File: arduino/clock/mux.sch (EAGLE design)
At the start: 53 parts, among them U1 SN74HC595N, U2 SN74HC595N, U3 SN74HC595N

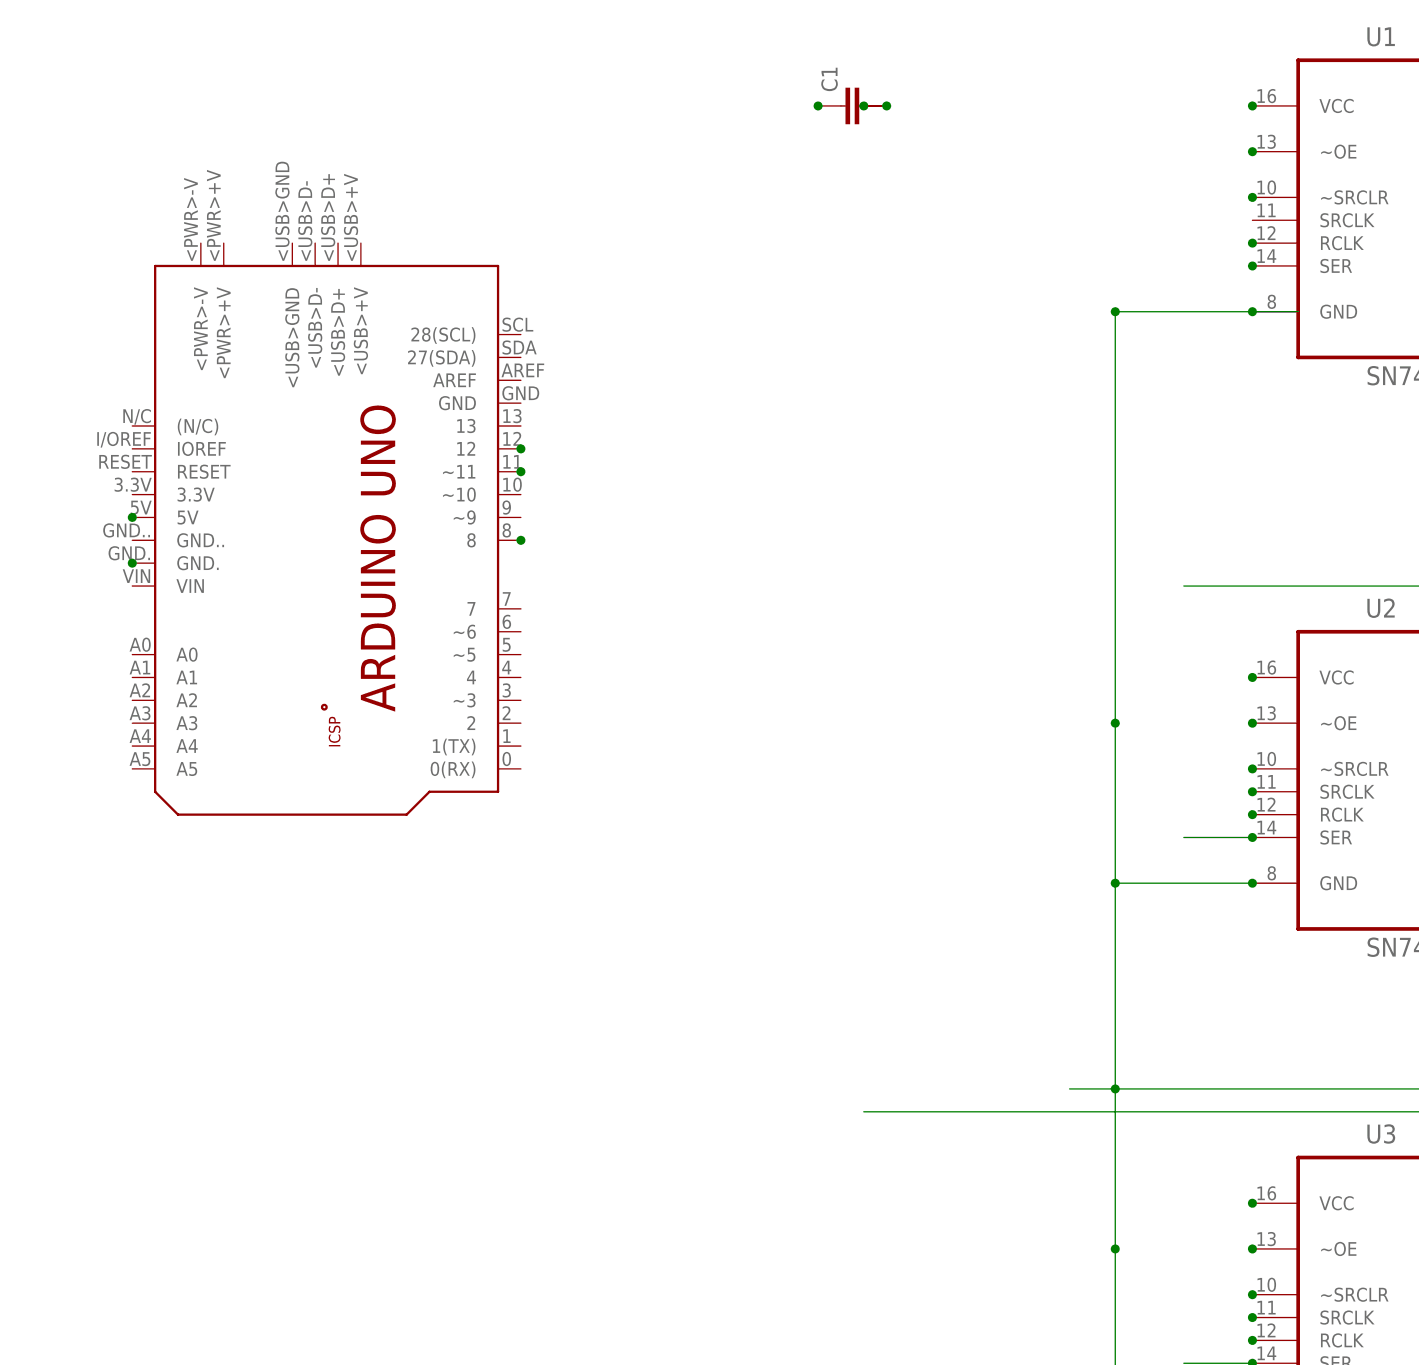
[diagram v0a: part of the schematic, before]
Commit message: Rewire +5V => VCC U{1,2,3}
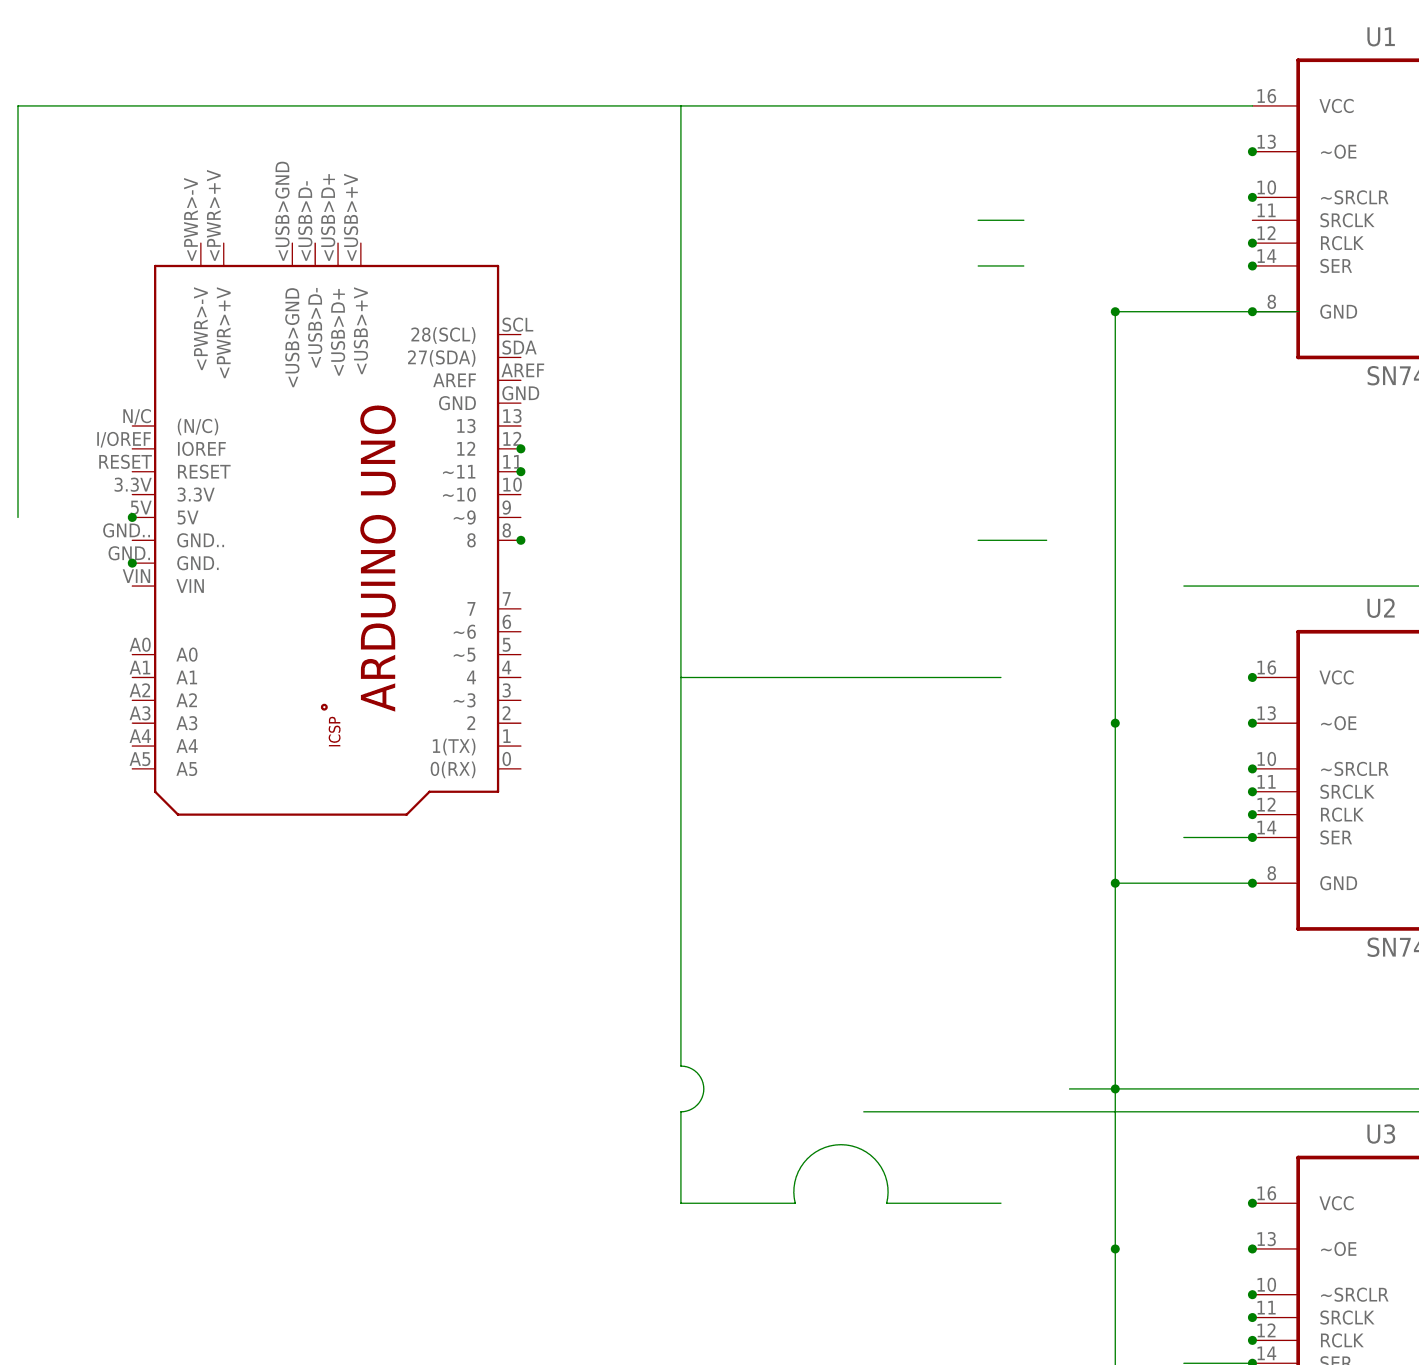
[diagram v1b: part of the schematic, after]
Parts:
- removed C1: (no value), capacitor-wima:C-10-15/6
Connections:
- removed net N$50: C1.1
- removed net N$51: C1.2
- removed net N$59: C1.3
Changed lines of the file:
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@@
 <part name="U3" library="SN74HC595N" deviceset="SN74HC595N" device=""/>
 <part name="PCB1" library="E14_Arduino_published" deviceset="ARDUINO_UNO" device=""/>
-<part name="C1" library="capacitor-wima" deviceset="C-" device="10-15/6"/>
 </parts>
 <sheets>
 <sheet>
 <plain>
-<wire x1="20.32" y1="60.96" x2="-7.62" y2="60.96" width="0.1524" layer="93"/>
-<wire x1="-7.62" y1="60.96" x2="-7.62" y2="53.34" width="0.1524" layer="93"/>
-<wire x1="-7.62" y1="53.34" x2="-7.62" y2="10.16" width="0.1524" layer="93"/>
-<wire x1="-7.62" y1="5.08" x2="-7.62" y2="-2.54" width="0.1524" layer="93"/>
 <wire x1="-7.62" y1="-2.54" x2="2.54" y2="-2.54" width="0.1524" layer="93"/>
 <wire x1="7.62" y1="-2.54" x2="20.32" y2="-2.54" width="0.1524" layer="93"/>
@@
 <wire x1="-116.84" y1="-48.26" x2="-116.84" y2="10.16" width="0.1524" layer="93"/>
 <wire x1="-116.84" y1="10.16" x2="-104.14" y2="10.16" width="0.1524" layer="93"/>
-<wire x1="-7.62" y1="-2.54" x2="-7.62" y2="-10.16" width="0.1524" layer="93"/>
-<wire x1="-7.62" y1="-10.16" x2="-7.62" y2="-60.96" width="0.1524" layer="93"/>
-<wire x1="-7.62" y1="-60.96" x2="-7.62" y2="-71.12" width="0.1524" layer="93"/>
-<wire x1="-116.84" y1="60.96" x2="-116.84" y2="15.24" width="0.1524" layer="93"/>
 <wire x1="-116.84" y1="15.24" x2="-101.6" y2="15.24" width="0.1524" layer="93"/>
-<wire x1="-116.84" y1="60.96" x2="-7.62" y2="60.96" width="0.1524" layer="93"/>
 <wire x1="20.32" y1="55.88" x2="5.08" y2="55.88" width="0.1524" layer="93"/>
 <wire x1="5.08" y1="55.88" x2="5.08" y2="53.34" width="0.1524" layer="93"/>
@@
 <wire x1="20.32" y1="-7.62" x2="5.08" y2="-7.62" width="0.1524" layer="93"/>
 <wire x1="20.32" y1="-66.04" x2="5.08" y2="-66.04" width="0.1524" layer="93"/>
-<wire x1="20.32" y1="-12.7" x2="7.62" y2="-12.7" width="0.1524" layer="93"/>
-<wire x1="2.54" y1="-12.7" x2="-2.54" y2="-12.7" width="0.1524" layer="93"/>
-<wire x1="20.32" y1="-71.12" x2="7.62" y2="-71.12" width="0.1524" layer="93"/>
-<wire x1="2.54" y1="-71.12" x2="-7.62" y2="-71.12" width="0.1524" layer="93"/>
 <wire x1="-7.62" y1="-60.96" x2="2.54" y2="-60.96" width="0.1524" layer="93"/>
 <wire x1="7.62" y1="-60.96" x2="20.32" y2="-60.96" width="0.1524" layer="93"/>
@@
 <wire x1="-22.86" y1="43.18" x2="-10.16" y2="43.18" width="0.1524" layer="93"/>
 <wire x1="-5.08" y1="43.18" x2="20.32" y2="43.18" width="0.1524" layer="93"/>
-<wire x1="-10.16" y1="43.18" x2="-5.08" y2="43.18" width="0.1524" layer="93" curve="-180"/>
 <wire x1="5.08" y1="53.34" x2="5.08" y2="48.26" width="0.1524" layer="93" curve="-180"/>
 <wire x1="5.08" y1="45.72" x2="5.08" y2="40.64" width="0.1524" layer="93" curve="-180"/>
 <wire x1="2.54" y1="-2.54" x2="7.62" y2="-2.54" width="0.1524" layer="93" curve="-180"/>
-<wire x1="2.54" y1="-12.7" x2="7.62" y2="-12.7" width="0.1524" layer="93" curve="-180"/>
 <wire x1="2.54" y1="-60.96" x2="7.62" y2="-60.96" width="0.1524" layer="93" curve="-180"/>
 <wire x1="12.7" y1="7.62" x2="-22.86" y2="7.62" width="0.1524" layer="93"/>
@@
 <wire x1="7.62" y1="-78.74" x2="12.7" y2="-78.74" width="0.1524" layer="93"/>
 <wire x1="2.54" y1="-78.74" x2="7.62" y2="-78.74" width="0.1524" layer="93" curve="-180"/>
-<wire x1="2.54" y1="-71.12" x2="7.62" y2="-71.12" width="0.1524" layer="93" curve="-180"/>
 <wire x1="-60.96" y1="22.86" x2="-25.4" y2="22.86" width="0.1524" layer="93"/>
 <wire x1="-25.4" y1="17.78" x2="-25.4" y2="-10.16" width="0.1524" layer="93"/>
@@
 <wire x1="2.54" y1="-15.24" x2="7.62" y2="-15.24" width="0.1524" layer="93" curve="-180"/>
 <wire x1="2.54" y1="-15.24" x2="-5.08" y2="-15.24" width="0.1524" layer="93"/>
-<wire x1="-7.62" y1="10.16" x2="-7.62" y2="5.08" width="0.1524" layer="93" curve="-180"/>
 <wire x1="20.32" y1="48.26" x2="-5.08" y2="48.26" width="0.1524" layer="93"/>
 <wire x1="-10.16" y1="48.26" x2="-25.4" y2="48.26" width="0.1524" layer="93"/>
 <wire x1="-25.4" y1="48.26" x2="-25.4" y2="22.86" width="0.1524" layer="93"/>
-<wire x1="-10.16" y1="48.26" x2="-5.08" y2="48.26" width="0.1524" layer="93" curve="-180"/>
-<wire x1="-7.62" y1="53.34" x2="-2.54" y2="53.34" width="0.1524" layer="93"/>
-<wire x1="-2.54" y1="53.34" x2="-2.54" y2="50.8" width="0.1524" layer="93"/>
-<wire x1="-2.54" y1="50.8" x2="20.32" y2="50.8" width="0.1524" layer="93"/>
-<wire x1="-7.62" y1="-10.16" x2="-2.54" y2="-10.16" width="0.1524" layer="93"/>
-<wire x1="-2.54" y1="-10.16" x2="-2.54" y2="-12.7" width="0.1524" layer="93"/>
 <wire x1="-25.4" y1="-10.16" x2="-15.24" y2="-10.16" width="0.1524" layer="93"/>
 <wire x1="-15.24" y1="-10.16" x2="-15.24" y2="-15.24" width="0.1524" layer="93"/>
@@
 <wire x1="10.16" y1="45.72" x2="20.32" y2="45.72" width="0.1524" layer="93"/>
 <wire x1="-27.94" y1="12.7" x2="-22.86" y2="12.7" width="0.1524" layer="93" curve="-180"/>
-<wire x1="-10.16" y1="12.7" x2="-5.08" y2="12.7" width="0.1524" layer="93" curve="-180"/>
 <wire x1="2.54" y1="12.7" x2="7.62" y2="12.7" width="0.1524" layer="93" curve="-180"/>
 <wire x1="10.16" y1="45.72" x2="10.16" y2="40.64" width="0.1524" layer="93" curve="-180"/>
@@
 <instance part="U3" gate="A" x="38.1" y="-68.58"/>
 <instance part="PCB1" gate="G$1" x="-81.28" y="12.7" rot="R270"/>
-<instance part="C1" gate="G$1" x="-25.4" y="60.96" rot="R90"/>
 </instances>
 <busses>
@@
 </segment>
 </net>
-<net name="N$48" class="0">
-<segment>
-<pinref part="U1" gate="A" pin="VCC"/>
-<junction x="20.32" y="60.96"/>
-</segment>
-</net>
 <net name="N$46" class="0">
 <segment>
@@
 <pinref part="PCB1" gate="G$1" pin="5V"/>
 <junction x="-104.14" y="15.24"/>
-</segment>
-</net>
-<net name="N$50" class="0">
-<segment>
-<pinref part="C1" gate="G$1" pin="1"/>
-<junction x="-27.94" y="60.96"/>
-</segment>
-</net>
-<net name="N$51" class="0">
-<segment>
-<pinref part="C1" gate="G$1" pin="2"/>
-<junction x="-20.32" y="60.96"/>
-</segment>
-</net>
-<net name="N$59" class="0">
-<segment>
-<pinref part="C1" gate="G$1" pin="3"/>
-<junction x="-22.86" y="60.96"/>
 </segment>
 </net>
@@
 </segment>
 </net>
+<net name="N$18" class="0">
+<segment>
+<wire x1="-10.16" y1="48.26" x2="-5.08" y2="48.26" width="0.1524" layer="91"/>
+</segment>
+</net>
+<net name="N$73" class="0">
+<segment>
+<wire x1="-10.16" y1="43.18" x2="-5.08" y2="43.18" width="0.1524" layer="91"/>
+</segment>
+</net>
+<net name="N$74" class="0">
+<segment>
+<wire x1="-10.16" y1="12.7" x2="-2.54" y2="12.7" width="0.1524" layer="91"/>
+</segment>
+</net>
+<net name="N$48" class="0">
+<segment>
+<pinref part="U1" gate="A" pin="VCC"/>
+<wire x1="20.32" y1="60.96" x2="-43.18" y2="60.96" width="0.1524" layer="91"/>
+<wire x1="-43.18" y1="60.96" x2="-43.18" y2="-2.54" width="0.1524" layer="91"/>
+<wire x1="-7.62" y1="-2.54" x2="-43.18" y2="-2.54" width="0.1524" layer="91"/>
+<wire x1="-43.18" y1="-2.54" x2="-43.18" y2="-45.72" width="0.1524" layer="91"/>
+<wire x1="-43.18" y1="-60.96" x2="-30.48" y2="-60.96" width="0.1524" layer="91"/>
+<wire x1="-30.48" y1="-60.96" x2="-20.32" y2="-60.96" width="0.1524" layer="91" curve="-208.072487"/>
+<wire x1="-20.32" y1="-60.96" x2="-7.62" y2="-60.96" width="0.1524" layer="91"/>
+<wire x1="-43.18" y1="-60.96" x2="-43.18" y2="-50.8" width="0.1524" layer="91"/>
+<wire x1="-43.18" y1="-45.72" x2="-43.18" y2="-50.8" width="0.1524" layer="91" curve="-180"/>
+<wire x1="-43.18" y1="60.96" x2="-116.84" y2="60.96" width="0.1524" layer="91"/>
+<wire x1="-116.84" y1="60.96" x2="-116.84" y2="15.24" width="0.1524" layer="91"/>
+</segment>
+</net>

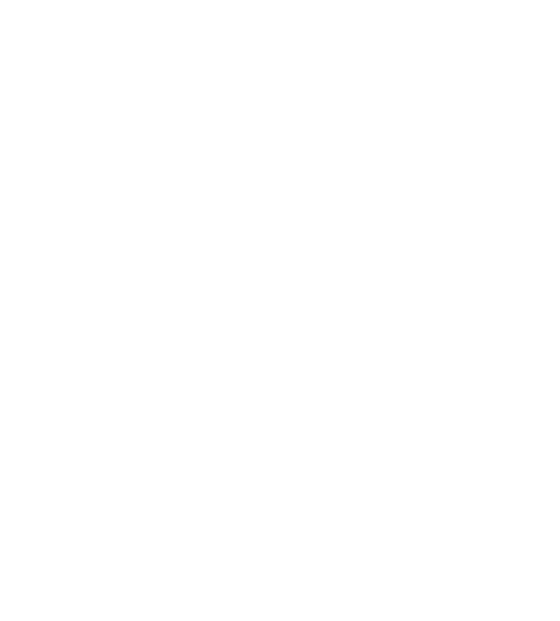
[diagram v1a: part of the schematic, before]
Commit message: Add ds1307
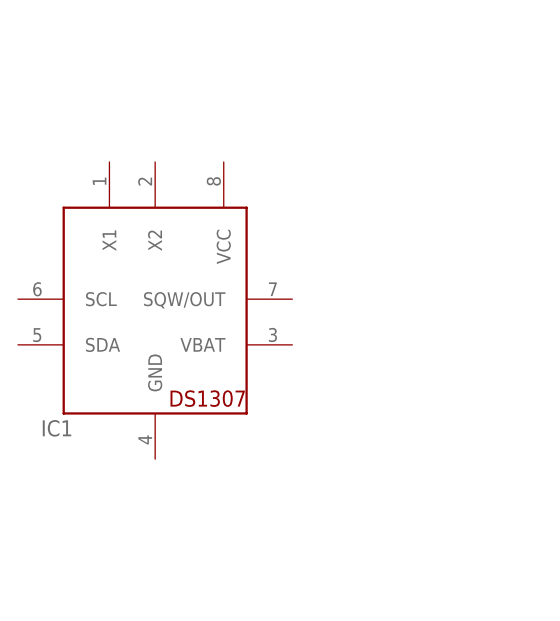
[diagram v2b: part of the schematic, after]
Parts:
- added IC1: DS1307, adafruit:DS1307
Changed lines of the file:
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@@
 <layer number="54" name="bGND_GNDA" color="1" fill="9" visible="no" active="no"/>
 <layer number="56" name="wert" color="7" fill="1" visible="no" active="no"/>
+<layer number="57" name="tCAD" color="7" fill="1" visible="no" active="no"/>
 <layer number="90" name="Modules" color="5" fill="1" visible="yes" active="yes"/>
 <layer number="91" name="Nets" color="2" fill="1" visible="yes" active="yes"/>
@@
 <layer number="97" name="Info" color="7" fill="1" visible="yes" active="yes"/>
 <layer number="98" name="Guide" color="6" fill="1" visible="yes" active="yes"/>
+<layer number="99" name="SpiceOrder" color="7" fill="1" visible="no" active="no"/>
 <layer number="100" name="Muster" color="7" fill="1" visible="no" active="no"/>
 <layer number="101" name="Patch_Top" color="12" fill="4" visible="yes" active="yes"/>
@@
 <layer number="106" name="bPlate" color="7" fill="1" visible="yes" active="yes"/>
 <layer number="107" name="Crop" color="7" fill="1" visible="yes" active="yes"/>
+<layer number="108" name="fp8" color="7" fill="1" visible="no" active="yes"/>
+<layer number="109" name="fp9" color="7" fill="1" visible="no" active="yes"/>
+<layer number="110" name="fp0" color="7" fill="1" visible="no" active="yes"/>
+<layer number="111" name="LPC17xx" color="7" fill="1" visible="no" active="yes"/>
+<layer number="112" name="tSilk" color="7" fill="1" visible="no" active="yes"/>
+<layer number="113" name="ReferenceLS" color="7" fill="1" visible="no" active="no"/>
 <layer number="116" name="Patch_BOT" color="9" fill="4" visible="yes" active="yes"/>
+<layer number="118" name="Rect_Pads" color="7" fill="1" visible="no" active="no"/>
 <layer number="121" name="_tsilk" color="7" fill="1" visible="yes" active="yes"/>
 <layer number="122" name="_bsilk" color="7" fill="1" visible="yes" active="yes"/>
+<layer number="123" name="tTestmark" color="7" fill="1" visible="no" active="yes"/>
+<layer number="124" name="bTestmark" color="7" fill="1" visible="no" active="yes"/>
 <layer number="125" name="_tNames" color="7" fill="1" visible="yes" active="yes"/>
+<layer number="126" name="_bNames" color="7" fill="1" visible="no" active="yes"/>
+<layer number="127" name="_tValues" color="7" fill="1" visible="no" active="yes"/>
+<layer number="128" name="_bValues" color="7" fill="1" visible="no" active="yes"/>
+<layer number="131" name="tAdjust" color="7" fill="1" visible="no" active="yes"/>
+<layer number="132" name="bAdjust" color="7" fill="1" visible="no" active="yes"/>
 <layer number="144" name="Drill_legend" color="7" fill="1" visible="yes" active="yes"/>
+<layer number="150" name="Notes" color="7" fill="1" visible="no" active="yes"/>
 <layer number="151" name="HeatSink" color="7" fill="1" visible="yes" active="yes"/>
+<layer number="152" name="_bDocu" color="7" fill="1" visible="no" active="yes"/>
+<layer number="153" name="FabDoc1" color="6" fill="1" visible="no" active="no"/>
+<layer number="154" name="FabDoc2" color="2" fill="1" visible="no" active="no"/>
+<layer number="155" name="FabDoc3" color="7" fill="15" visible="no" active="no"/>
+<layer number="199" name="Contour" color="7" fill="1" visible="no" active="yes"/>
 <layer number="200" name="200bmp" color="1" fill="10" visible="yes" active="yes"/>
 <layer number="201" name="201bmp" color="2" fill="10" visible="yes" active="yes"/>
@@
 <layer number="223" name="223bmp" color="24" fill="1" visible="no" active="no"/>
 <layer number="224" name="224bmp" color="25" fill="1" visible="no" active="no"/>
+<layer number="231" name="Eagle3D_PG1" color="7" fill="1" visible="no" active="no"/>
+<layer number="232" name="Eagle3D_PG2" color="7" fill="1" visible="no" active="no"/>
+<layer number="233" name="Eagle3D_PG3" color="7" fill="1" visible="no" active="no"/>
+<layer number="248" name="Housing" color="7" fill="1" visible="no" active="yes"/>
+<layer number="249" name="Edge" color="7" fill="1" visible="no" active="yes"/>
 <layer number="250" name="Descript" color="3" fill="1" visible="no" active="no"/>
 <layer number="251" name="SMDround" color="12" fill="11" visible="no" active="no"/>
@@
 <part name="U3" library="SN74HC595N" deviceset="SN74HC595N" device=""/>
 <part name="PCB1" library="E14_Arduino_published" deviceset="ARDUINO_UNO" device=""/>
+<part name="IC1" library="adafruit" deviceset="DS1307" device=""/>
 </parts>
 <sheets>
@@
 <wire x1="-7.62" y1="-2.54" x2="2.54" y2="-2.54" width="0.1524" layer="93"/>
 <wire x1="7.62" y1="-2.54" x2="20.32" y2="-2.54" width="0.1524" layer="93"/>
-<wire x1="0" y1="-48.26" x2="-116.84" y2="-48.26" width="0.1524" layer="93"/>
-<wire x1="-116.84" y1="-48.26" x2="-116.84" y2="10.16" width="0.1524" layer="93"/>
-<wire x1="-116.84" y1="10.16" x2="-104.14" y2="10.16" width="0.1524" layer="93"/>
+<wire x1="0" y1="-48.26" x2="-241.3" y2="-48.26" width="0.1524" layer="93"/>
+<wire x1="-241.3" y1="-48.26" x2="-241.3" y2="10.16" width="0.1524" layer="93"/>
+<wire x1="-241.3" y1="10.16" x2="-104.14" y2="10.16" width="0.1524" layer="93"/>
 <wire x1="-116.84" y1="15.24" x2="-101.6" y2="15.24" width="0.1524" layer="93"/>
 <wire x1="20.32" y1="55.88" x2="5.08" y2="55.88" width="0.1524" layer="93"/>
@@
 <instance part="U3" gate="A" x="38.1" y="-68.58"/>
 <instance part="PCB1" gate="G$1" x="-81.28" y="12.7" rot="R270"/>
+<instance part="IC1" gate="G$1" x="-172.72" y="-17.78"/>
 </instances>
 <busses>
